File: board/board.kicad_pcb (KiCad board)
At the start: 2 copper layers, 46 x 9 mm, 3 parts, among them U1 BK-6223-TR, U2 BK-6223-TR

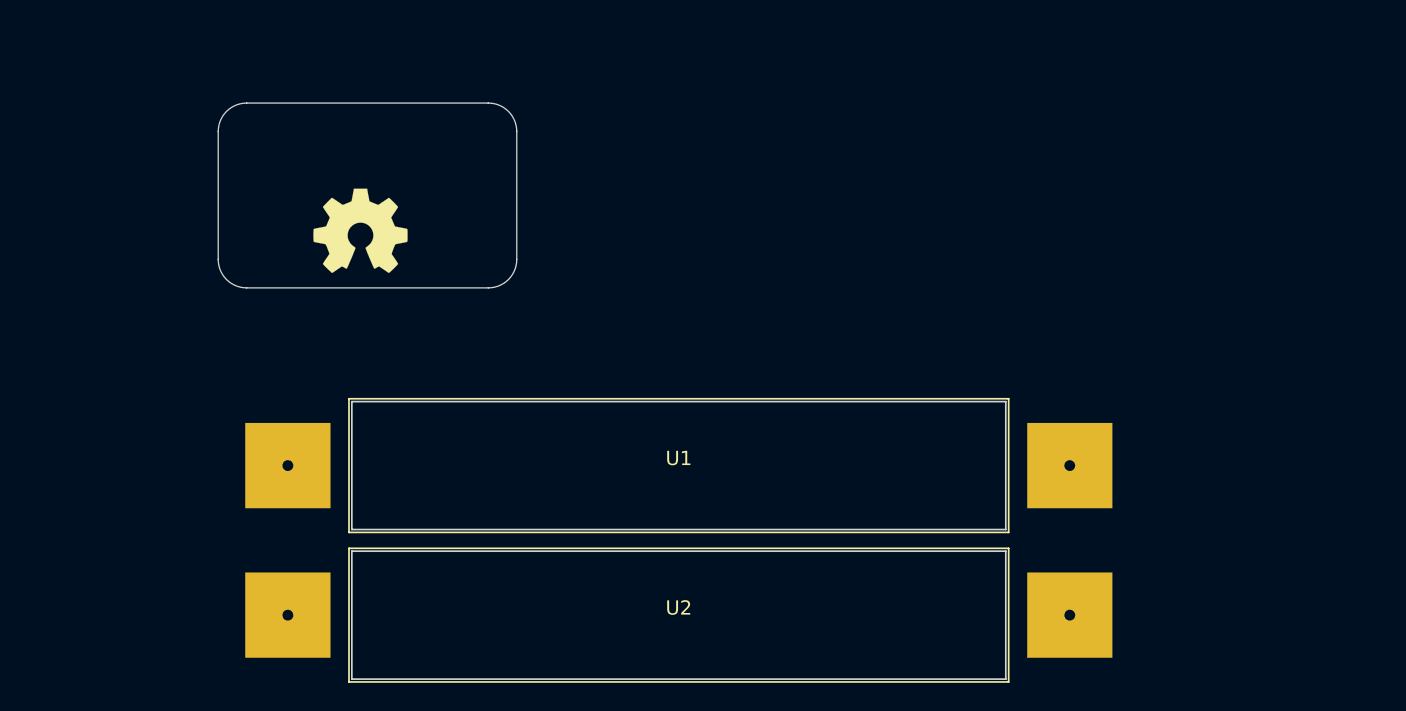
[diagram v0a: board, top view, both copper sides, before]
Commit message: added custom footprint
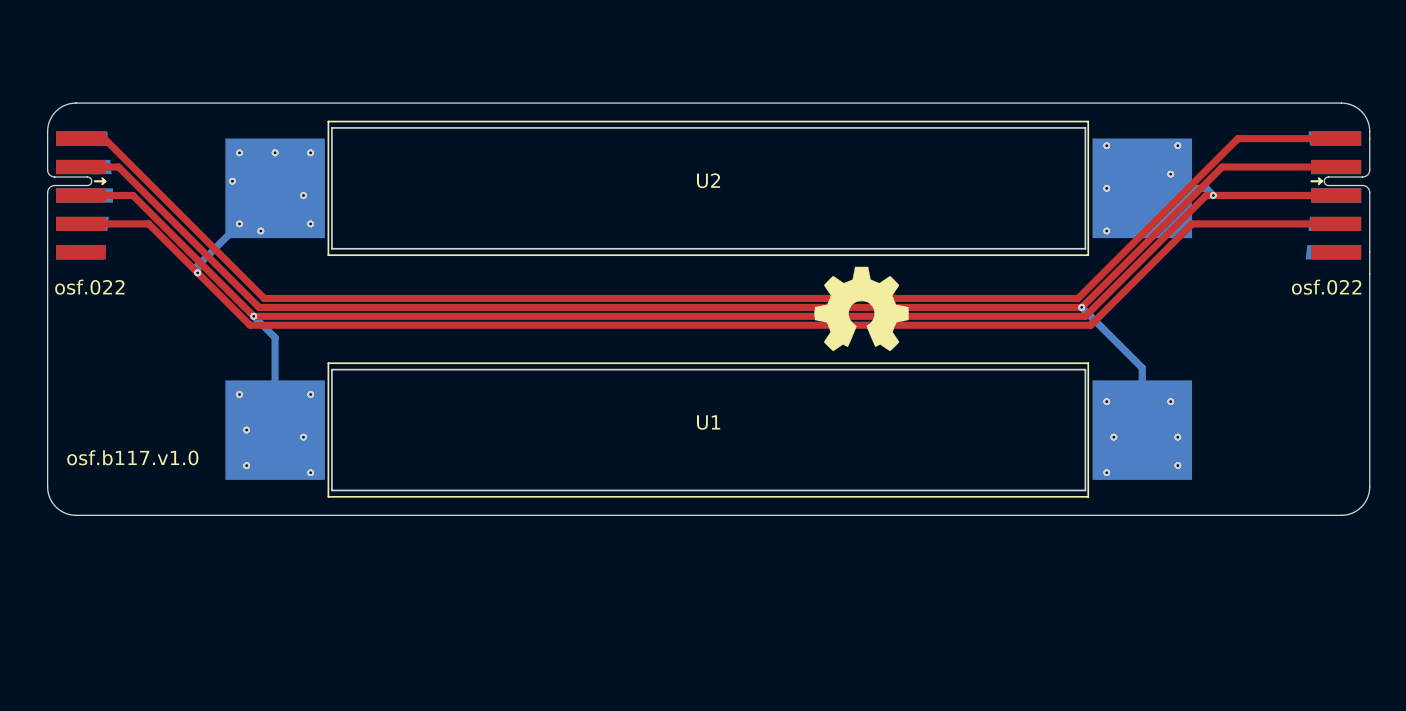
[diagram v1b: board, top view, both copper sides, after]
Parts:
- added J1: 022_battery_cells, on_edge:on_edge_2x05_device, F.Cu at (128.0, 96.5)
- added J2: 022_battery_cells, on_edge:on_edge_2x05_host, F.Cu at (221.0, 96.5)
- moved LOGO1 35.7 mm to (185.2, 104.5)
- moved U2 30.1 mm to (174.5, 96.0)
- moved U1 3.26 mm to (174.5, 113.0)
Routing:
- net /2x_aaa/Mid: track 0.00 -> 109.2 mm, vias 0 -> 13
- net /2x_aaa/Low: track 0.00 -> 106.9 mm, vias 0 -> 7
- net /2x_aaa/High: track 0.00 -> 102.4 mm, vias 0 -> 9
- net GND: track 0.00 -> 97.6 mm
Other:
- board size 46 x 9 mm -> 93 x 29 mm
- board text added: "osf.022"
- board text added: "osf.b117.v1.0"

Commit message: added silkscreen + and - so that the pattery polarization is clear. added resistor for connection to GND if needed
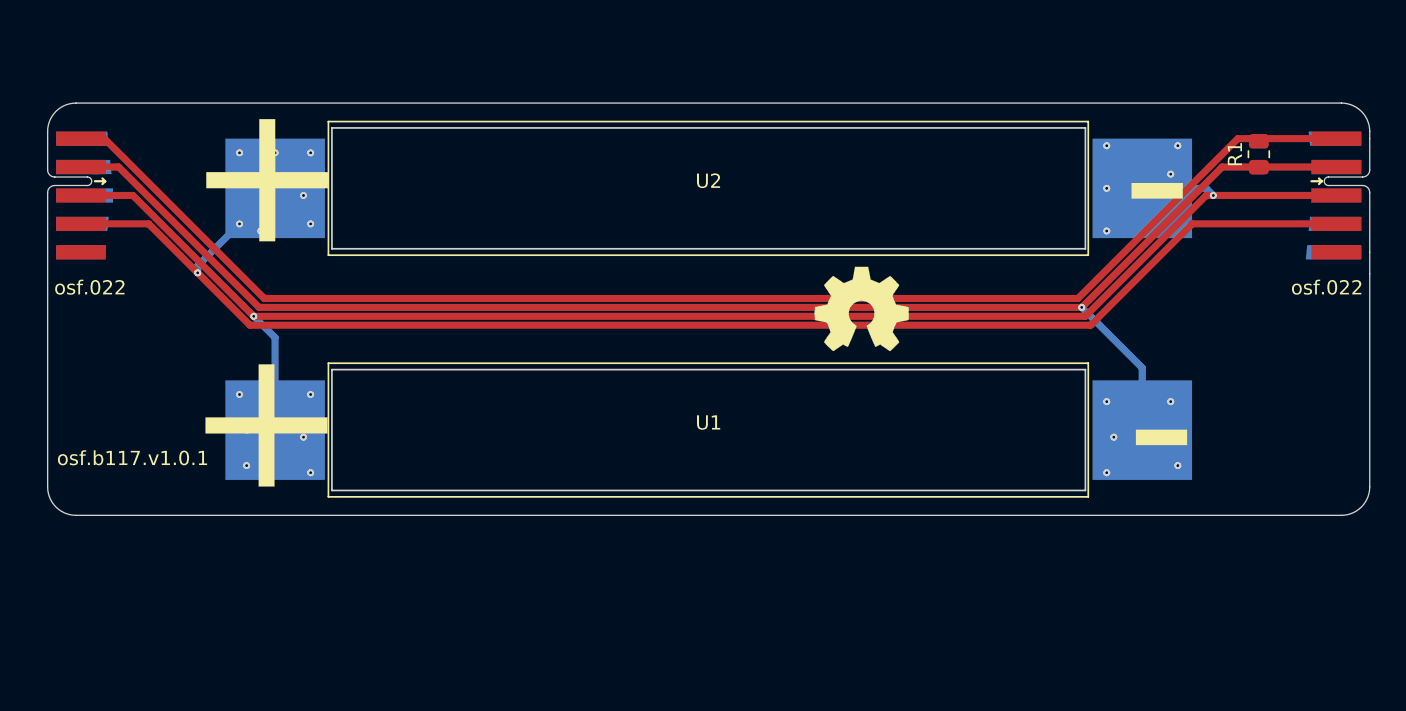
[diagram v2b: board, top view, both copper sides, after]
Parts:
- added R1: d.n.p, Resistor_SMD:R_0805_2012Metric, F.Cu at (213.2, 93.6)
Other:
- board text added: "+"
- board text added: "-"
- board text added: "osf.b117.v1.0.1"
- board text removed: "osf.b117.v1.0"
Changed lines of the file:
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@@
   (net 7 "unconnected-(J2-Pad5)")
   (net 8 "unconnected-(J2-Pad6)")
+  (footprint "Resistor_SMD:R_0805_2012Metric" (layer "F.Cu")
+    (at 213.2 93.6 90)
+    (descr "Resistor SMD 0805 (2012 Metric), square (rectangular) end terminal, IPC_7351 nominal, (Body size source: IPC-SM-782 page 72, https://www.pcb-3d.com/wordpress/wp-content/uploads/ipc-sm-782a_amendment_1_and_2.pdf), generated with kicad-footprint-generator")
+    (tags "resistor")
+    (property "Sheetfile" "board.kicad_sch")
+    (property "Sheetname" "")
+    (attr smd)
+    (fp_text reference "R1" (at 0 -1.65 90) (layer "F.SilkS")
+      (effects (font (size 1 1) (thickness 0.15)))
+    )
+    (fp_text value "d.n.p" (at 0 1.65 90) (layer "F.Fab")
+      (effects (font (size 1 1) (thickness 0.15)))
+    )
+    (fp_text user "${REFERENCE}" (at 0 0 90) (layer "F.Fab")
+      (effects (font (size 0.5 0.5) (thickness 0.08)))
+    )
+    (fp_line (start -0.227064 -0.735) (end 0.227064 -0.735) (layer "F.SilkS") (width 0.12))
+    (fp_line (start -0.227064 0.735) (end 0.227064 0.735) (layer "F.SilkS") (width 0.12))
+    (fp_line (start 1.68 0.95) (end -1.68 0.95) (layer "F.CrtYd") (width 0.05))
+    (fp_line (start -1.68 0.95) (end -1.68 -0.95) (layer "F.CrtYd") (width 0.05))
+    (fp_line (start 1.68 -0.95) (end 1.68 0.95) (layer "F.CrtYd") (width 0.05))
+    (fp_line (start -1.68 -0.95) (end 1.68 -0.95) (layer "F.CrtYd") (width 0.05))
+    (fp_line (start -1 -0.625) (end 1 -0.625) (layer "F.Fab") (width 0.1))
+    (fp_line (start -1 0.625) (end -1 -0.625) (layer "F.Fab") (width 0.1))
+    (fp_line (start 1 0.625) (end -1 0.625) (layer "F.Fab") (width 0.1))
+    (fp_line (start 1 -0.625) (end 1 0.625) (layer "F.Fab") (width 0.1))
+    (pad "1" smd roundrect (at -0.9125 0 90) (size 1.025 1.4) (layers "F.Cu" "F.Paste" "F.Mask") (roundrect_rratio 0.243902)
+      (net 1 "/2x_aaa/Low") (pintype "passive"))
+    (pad "2" smd roundrect (at 0.9125 0 90) (size 1.025 1.4) (layers "F.Cu" "F.Paste" "F.Mask") (roundrect_rratio 0.243902)
+      (net 4 "GND") (pintype "passive"))
+    (model "${KICAD6_3DMODEL_DIR}/Resistor_SMD.3dshapes/R_0805_2012Metric.wrl"
+      (offset (xyz 0 0 0))
+      (scale (xyz 1 1 1))
+      (rotate (xyz 0 0 0))
+    )
+  )
   (footprint "Symbol:OSHW-Symbol_6.7x6mm_SilkScreen" (layer "F.Cu")
     (at 185.25 104.5)
@@
     (effects (font (size 1 1) (thickness 0.15)))
   )
+  (gr_text "+" (at 143.45 95.1) (layer "F.SilkS")
+    (effects (font (size 10 10) (thickness 0.5)))
+  )
+  (gr_text "-" (at 206.05 95.3) (layer "F.SilkS")
+    (effects (font (size 10 10) (thickness 0.5)))
+  )
   (gr_text "osf.022" (at 218 103) (layer "F.SilkS")
     (effects (font (size 1 1) (thickness 0.15)))
   )
-  (gr_text "osf.b117.v1.0" (at 134 115) (layer "F.SilkS")
+  (gr_text "-" (at 206.35 112.65) (layer "F.SilkS")
+    (effects (font (size 10 10) (thickness 0.5)))
+  )
+  (gr_text "+" (at 143.4 112.35) (layer "F.SilkS")
+    (effects (font (size 10 10) (thickness 0.5)))
+  )
+  (gr_text "osf.b117.v1.0.1" (at 134 115) (layer "F.SilkS")
     (effects (font (size 1 1) (thickness 0.15)))
   )
